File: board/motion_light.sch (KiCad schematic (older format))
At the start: 14 parts, among them CON1 AVR-ISP-6, J1 MOTION, J2 Conn_02x03_Counter_Clockwise, SW1 SW_Push, SW2 SW_Push, U1 ATTINY84-SSU, U2 APA102, U3 APA102, U4 PIR_MODULE

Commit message: Schematic revisions
* Add BoM details
* Add pull-down resistor on motion detector module
* Change GPIO header to 1x5
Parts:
- removed J2: Conn_02x03_Counter_Clockwise, Pin_Headers:Pin_Header_Straight_2x03_Pitch2.54mm, symbol Conn_02x03_Counter_Clockwise
- added J2: Conn_01x05, Pin_Headers:Pin_Header_Straight_1x05_Pitch2.54mm, symbol Conn_01x05
- added R4: 68.1K, Resistors_SMD:R_0805_HandSoldering, symbol R
- BT1: MFR (none) -> Keystone Electronics; MPN (none) -> 2464; SPN (none) -> 36-2464-ND; SPR (none) -> Digikey; SPURL (none) -> -
- CON1: MFR (none) -> Harwin Inc.; MPN (none) -> M20-9980345; SPN (none) -> 952-2120-ND; SPR (none) -> Digikey; SPURL (none) -> -
- D1: MFR (none) -> -; MPN (none) -> -; SPN (none) -> -; SPR (none) -> -; SPURL (none) -> -
- J1: MFR (none) -> Sullins Connector Solutions; MPN (none) -> PRPC040SBAN-M71RC; SPN (none) -> S1111EC-40-ND; SPR (none) -> Digikey; SPURL (none) -> -
- R1: MFR (none) -> Luna Optoelectronics; MPN (none) -> PDV-P8103; SPN (none) -> PDV-P8103-ND; SPR (none) -> Digikey; SPURL (none) -> -
- R2: MFR (none) -> Stackpole; MPN (none) -> RNCP0805FTD10K0; SPN (none) -> RNCP0805FTD10K0CT-ND; SPR (none) -> Digikey; SPURL (none) -> -
- R3: MFR (none) -> Stackpole; MPN (none) -> RNCP0805FTD1K00; SPN (none) -> RNCP0805FTD1K00CT-ND; SPR (none) -> Digikey; SPURL (none) -> -
- SW1, SW2: footprint Buttons_Switches_THT:SW_PUSH_6mm -> Buttons_Switches_THT:SW_Tactile_SPST_Angled_PTS645Vx83-2LFS; MFR (none) -> C&K; MPN (none) -> PTS645VH83-2 LFS; SPN (none) -> CKN9121-ND; SPR (none) -> Digikey; SPURL (none) -> -
- U1: value ATTINY84-SSU -> ATTINY84A-SSU; symbol ATTINY84-20SSU -> ATTINY84A-SSU; MFR (none) -> Microchip Technology; MPN (none) -> ATTINY84A-SSUR; SPN (none) -> ATTINY84A-SSURCT-ND; SPR (none) -> Digikey; SPURL (none) -> -
- U2, U3: MFR (none) -> -; MPN (none) -> APA102C; SPN (none) -> -; SPR (none) -> Ali Express; SPURL (none) -> -
- U4: MFR (none) -> Panasonic; MPN (none) -> EKMC1601111; SPN (none) -> 255-3074-ND; SPR (none) -> Digikey; SPURL (none) -> -
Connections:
- wire segments 44 -> 45

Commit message: Correct parts in BoM
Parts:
- R4: SPN RNCP0805FTD10K0CT-ND -> RNCP0805FTD68K1CT-ND
- SW1, SW2: MPN PTS645VH83-2 LFS -> PTS645VL83-2 LFS; SPN CKN9121-ND -> CKN9123-ND
- U4: MPN EKMC1601111 -> EKMC1603112; SPN 255-3074-ND -> 255-3087-ND
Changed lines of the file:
@@
 F 3 "http://www.ckswitches.com/media/1471/pts645.pdf" H 5650 950 50 0001 C CNN
 F 4 "C&K" H 0 0 50 0001 C CNN "MFR"
-F 5 "PTS645VH83-2 LFS" H 0 0 50 0001 C CNN "MPN"
-F 6 "Digikey" H 0 0 50 0001 C CNN "SPR"
-F 7 "CKN9121-ND" H 0 0 50 0001 C CNN "SPN"
+F 5 "PTS645VL83-2 LFS" H 0 0 50 0001 C CNN "MPN"
+F 6 "Digikey" H 0 0 50 0001 C CNN "SPR"
+F 7 "CKN9123-ND" H 0 0 50 0001 C CNN "SPN"
 F 8 "-" H 0 0 50 0001 C CNN "SPURL"
 	1    5650 750
@@
 F 3 "http://www3.panasonic.biz/ac/e_download/control/sensor/human/catalog/bltn_eng_papirs.pdf" H 4050 2600 60 0001 C CNN
 F 4 "Panasonic" H 0 0 50 0001 C CNN "MFR"
-F 5 "EKMC1601111" H 0 0 50 0001 C CNN "MPN"
-F 6 "Digikey" H 0 0 50 0001 C CNN "SPR"
-F 7 "255-3074-ND" H 0 0 50 0001 C CNN "SPN"
+F 5 "EKMC1603112" H 0 0 50 0001 C CNN "MPN"
+F 6 "Digikey" H 0 0 50 0001 C CNN "SPR"
+F 7 "255-3087-ND" H 0 0 50 0001 C CNN "SPN"
 F 8 "-" H 0 0 50 0001 C CNN "SPURL"
 	1    4050 2600
@@
 F 3 "http://www.ckswitches.com/media/1471/pts645.pdf" H 5650 1400 50 0001 C CNN
 F 4 "C&K" H 0 0 50 0001 C CNN "MFR"
-F 5 "PTS645VH83-2 LFS" H 0 0 50 0001 C CNN "MPN"
-F 6 "Digikey" H 0 0 50 0001 C CNN "SPR"
-F 7 "CKN9121-ND" H 0 0 50 0001 C CNN "SPN"
+F 5 "PTS645VL83-2 LFS" H 0 0 50 0001 C CNN "MPN"
+F 6 "Digikey" H 0 0 50 0001 C CNN "SPR"
+F 7 "CKN9123-ND" H 0 0 50 0001 C CNN "SPN"
 F 8 "-" H 0 0 50 0001 C CNN "SPURL"
 	1    5650 1200
@@
 F 5 "RNCP0805FTD68K1" H 0 0 50 0001 C CNN "MPN"
 F 6 "Digikey" H 0 0 50 0001 C CNN "SPR"
-F 7 "RNCP0805FTD10K0CT-ND" H 0 0 50 0001 C CNN "SPN"
+F 7 "RNCP0805FTD68K1CT-ND" H 0 0 50 0001 C CNN "SPN"
 F 8 "-" H 0 0 50 0001 C CNN "SPURL"
 	1    4500 2000

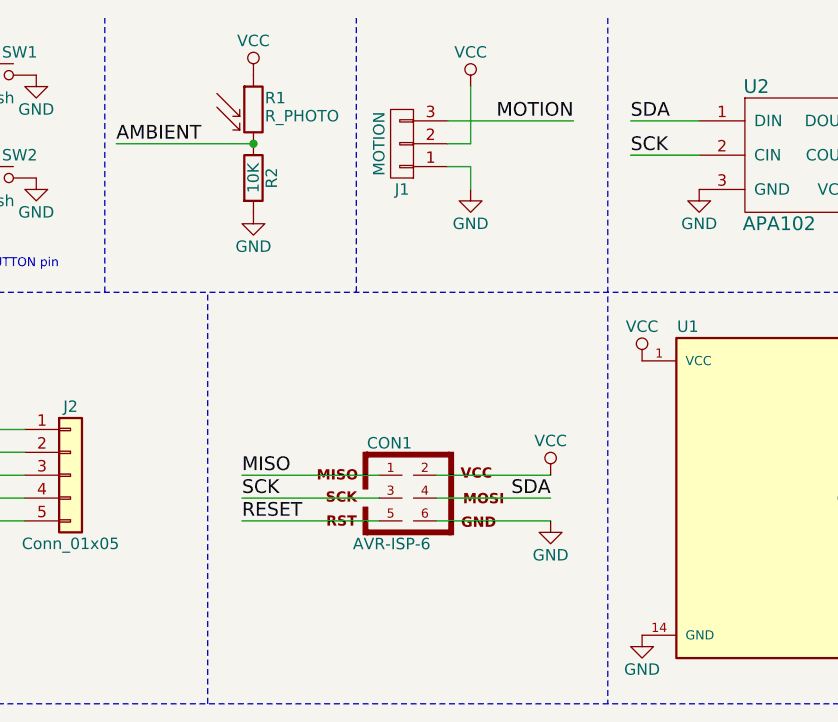
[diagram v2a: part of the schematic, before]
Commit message: Add decoupling cap
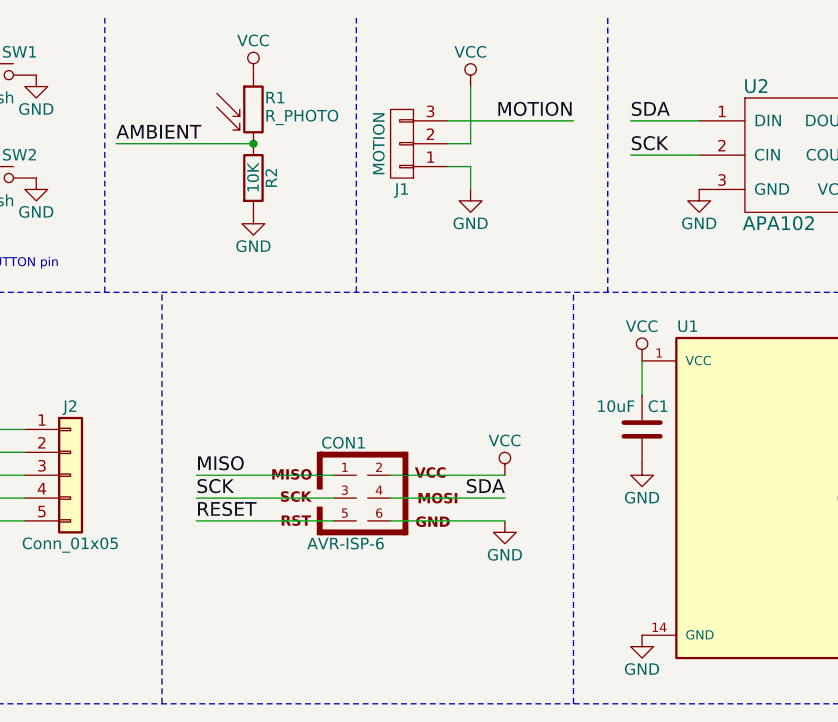
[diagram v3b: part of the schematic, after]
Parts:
- added C1: 10uF, Capacitors_SMD:C_0805_HandSoldering, symbol C
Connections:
- net GND: now also C1.2
- net VCC: now also C1.1
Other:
- moved on the sheet: CON1

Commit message: Schematic changes of unknown variety
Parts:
- added Q1: BSS83P, TO_SOT_Packages_SMD:SOT-23, symbol BSS83P
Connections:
- net VCC: now also Q1.2 (S); no longer R1.1, U2.4 (VCC), U3.4 (VCC)
- net PA3 renamed ACC_PWR
- net ACC_PWR: now also R1.1, U2.4 (VCC), U3.4 (VCC), Q1.3 (D); no longer U1.10 ((PCINT3/T0/ADC3)PA3)
- new net ~ACC_PWR_EN: Q1.1 (G), U1.10 ((PCINT3/T0/ADC3)PA3)
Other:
- moved on the sheet: C1

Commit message: Moar schematic changes
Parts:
- added J3: USB_OTG, Connectors_USB:USB_Micro-B_Molex-105017-0001, symbol USB_OTG
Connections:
- net ACC_PWR: now also J1.2 (P2), U4.1 (VDD)
- net GND: now also J3.5 (GND), J3.6 (Shield)
- net VCC: now also J3.1 (VBUS); no longer J1.2 (P2), U4.1 (VDD)
- no-connect marks 2 -> 5
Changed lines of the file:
@@
 $EndComp
 $Comp
-L GND #PWR10
+L GND #PWR01
 U 1 1 59B440F3
 P 5850 750
-F 0 "#PWR10" H 5850 500 50  0001 C CNN
+F 0 "#PWR01" H 5850 500 50  0001 C CNN
 F 1 "GND" H 5850 600 50  0000 C CNN
 F 2 "" H 5850 750 50  0001 C CNN
@@
 $EndComp
 $Comp
-L VCC #PWR17
+L VCC #PWR02
 U 1 1 59B443A5
 P 8500 2000
-F 0 "#PWR17" H 8500 1850 50  0001 C CNN
+F 0 "#PWR02" H 8500 1850 50  0001 C CNN
 F 1 "VCC" H 8500 2150 50  0000 C CNN
 F 2 "" H 8500 2000 50  0001 C CNN
@@
 $EndComp
 $Comp
-L GND #PWR18
+L GND #PWR03
 U 1 1 59B443C3
 P 8500 3200
-F 0 "#PWR18" H 8500 2950 50  0001 C CNN
+F 0 "#PWR03" H 8500 2950 50  0001 C CNN
 F 1 "GND" H 8500 3050 50  0000 C CNN
 F 2 "" H 8500 3200 50  0001 C CNN
@@
 $EndComp
 $Comp
-L VCC #PWR13
-U 1 1 59B44512
-P 7750 800
-F 0 "#PWR13" H 7750 650 50  0001 C CNN
-F 1 "VCC" H 7750 950 50  0000 C CNN
-F 2 "" H 7750 800 50  0001 C CNN
-F 3 "" H 7750 800 50  0001 C CNN
-	1    7750 800
-	1    0    0    -1
-$EndComp
-$Comp
-L GND #PWR14
+L GND #PWR04
 U 1 1 59B44548
 P 7750 1250
-F 0 "#PWR14" H 7750 1000 50  0001 C CNN
+F 0 "#PWR04" H 7750 1000 50  0001 C CNN
 F 1 "GND" H 7750 1100 50  0000 C CNN
 F 2 "" H 7750 1250 50  0001 C CNN
@@
 $EndComp
 $Comp
-L VCC #PWR15
+L VCC #PWR05
 U 1 1 59B44758
 P 7900 2500
-F 0 "#PWR15" H 7900 2350 50  0001 C CNN
+F 0 "#PWR05" H 7900 2350 50  0001 C CNN
 F 1 "VCC" H 7900 2650 50  0000 C CNN
 F 2 "" H 7900 2500 50  0001 C CNN
@@
 $EndComp
 $Comp
-L GND #PWR16
+L GND #PWR06
 U 1 1 59B44778
 P 7900 2700
-F 0 "#PWR16" H 7900 2450 50  0001 C CNN
+F 0 "#PWR06" H 7900 2450 50  0001 C CNN
 F 1 "GND" H 7900 2550 50  0000 C CNN
 F 2 "" H 7900 2700 50  0001 C CNN
@@
 $EndComp
 $Comp
-L VCC #PWR5
+L VCC #PWR07
 U 1 1 59B46B1F
 P 4550 850
-F 0 "#PWR5" H 4550 700 50  0001 C CNN
+F 0 "#PWR07" H 4550 700 50  0001 C CNN
 F 1 "VCC" H 4550 1000 50  0000 C CNN
 F 2 "" H 4550 850 50  0001 C CNN
@@
 $EndComp
 $Comp
-L GND #PWR6
+L GND #PWR08
 U 1 1 59B46B41
 P 4550 1250
-F 0 "#PWR6" H 4550 1000 50  0001 C CNN
+F 0 "#PWR08" H 4550 1000 50  0001 C CNN
 F 1 "GND" H 4550 1100 50  0000 C CNN
 F 2 "" H 4550 1250 50  0001 C CNN
@@
 $EndComp
 $Comp
-L GND #PWR12
+L GND #PWR09
 U 1 1 59B47FCA
 P 6800 1350
-F 0 "#PWR12" H 6800 1100 50  0001 C CNN
+F 0 "#PWR09" H 6800 1100 50  0001 C CNN
 F 1 "GND" H 6800 1200 50  0000 C CNN
 F 2 "" H 6800 1350 50  0001 C CNN
@@
 $EndComp
 $Comp
-L VCC #PWR8
+L VCC #PWR010
 U 1 1 59E6DA53
 P 5350 2300
-F 0 "#PWR8" H 5350 2150 50  0001 C CNN
+F 0 "#PWR010" H 5350 2150 50  0001 C CNN
 F 1 "VCC" H 5350 2450 50  0000 C CNN
 F 2 "" H 5350 2300 50  0001 C CNN
@@
 $EndComp
 $Comp
-L GND #PWR9
+L GND #PWR011
 U 1 1 59E6DA7B
 P 5350 2700
-F 0 "#PWR9" H 5350 2450 50  0001 C CNN
+F 0 "#PWR011" H 5350 2450 50  0001 C CNN
 F 1 "GND" H 5350 2550 50  0000 C CNN
 F 2 "" H 5350 2700 50  0001 C CNN
@@
 $EndComp
 $Comp
-L GND #PWR2
+L GND #PWR012
 U 1 1 59E6E9D6
 P 4100 1450
-F 0 "#PWR2" H 4100 1200 50  0001 C CNN
+F 0 "#PWR012" H 4100 1200 50  0001 C CNN
 F 1 "GND" H 4100 1300 50  0000 C CNN
 F 2 "" H 4100 1450 50  0001 C CNN
@@
 $EndComp
 $Comp
-L VCC #PWR3
-U 1 1 59E6F86C
-P 4500 2500
-F 0 "#PWR3" H 4500 2350 50  0001 C CNN
-F 1 "VCC" H 4500 2650 50  0000 C CNN
-F 2 "" H 4500 2500 50  0001 C CNN
-F 3 "" H 4500 2500 50  0001 C CNN
-	1    4500 2500
-	1    0    0    -1
-$EndComp
-$Comp
-L GND #PWR4
+L GND #PWR013
 U 1 1 59E6F89A
 P 4500 2700
-F 0 "#PWR4" H 4500 2450 50  0001 C CNN
+F 0 "#PWR013" H 4500 2450 50  0001 C CNN
 F 1 "GND" H 4500 2550 50  0000 C CNN
 F 2 "" H 4500 2700 50  0001 C CNN
@@
 $EndComp
 $Comp
-L GND #PWR11
+L GND #PWR014
 U 1 1 59E75359
 P 5850 1200
-F 0 "#PWR11" H 5850 950 50  0001 C CNN
+F 0 "#PWR014" H 5850 950 50  0001 C CNN
 F 1 "GND" H 5850 1050 50  0000 C CNN
 F 2 "" H 5850 1200 50  0001 C CNN
@@
 $EndComp
 $Comp
-L GND #PWR7
+L GND #PWR015
 U 1 1 59F51723
 P 4650 2000
-F 0 "#PWR7" H 4650 1750 50  0001 C CNN
+F 0 "#PWR015" H 4650 1750 50  0001 C CNN
 F 1 "GND" H 4650 1850 50  0000 C CNN
 F 2 "" H 4650 2000 50  0001 C CNN
@@
 	7650 950  8200 950
 Wire Wire Line
-	7650 1050 7750 1050
-Wire Wire Line
-	7750 1050 7750 800
+	7650 1050 8200 1050
 Wire Wire Line
 	7650 1150 7750 1150
@@
 	4950 1700 4950 500
 Wire Notes Line
-	3750 3500 11200 3500
+	2050 3500 11200 3500
 Wire Notes Line
 	6400 3500 6400 1700
@@
 	3950 2000 4350 2000
 Wire Wire Line
-	5800 2700 5450 2700
-Wire Wire Line
-	5450 2700 5350 2700
+	5350 2700 5800 2700
 Connection ~ 6800 1050
 Wire Wire Line
@@
 	9800 1250 9800 650
 $Comp
-L GND #PWR19
+L GND #PWR016
 U 1 1 59B441B9
 P 8750 1250
-F 0 "#PWR19" H 8750 1000 50  0001 C CNN
+F 0 "#PWR016" H 8750 1000 50  0001 C CNN
 F 1 "GND" H 8750 1100 50  0000 C CNN
 F 2 "" H 8750 1250 50  0001 C CNN
@@
 $EndComp
 $Comp
-L GND #PWR20
+L GND #PWR017
 U 1 1 59B4419D
 P 10000 1250
-F 0 "#PWR20" H 10000 1000 50  0001 C CNN
+F 0 "#PWR017" H 10000 1000 50  0001 C CNN
 F 1 "GND" H 10000 1100 50  0000 C CNN
 F 2 "" H 10000 1250 50  0001 C CNN
@@
 $EndComp
 $Comp
-L VCC #PWR1
+L VCC #PWR018
 U 1 1 5A543B0A
 P 3050 1250
-F 0 "#PWR1" H 3050 1100 50  0001 C CNN
+F 0 "#PWR018" H 3050 1100 50  0001 C CNN
 F 1 "VCC" H 3050 1400 50  0000 C CNN
 F 2 "" H 3050 1250 50  0001 C CNN
@@
 $EndComp
 Wire Wire Line
-	11050 650  9800 650
-Wire Wire Line
-	9800 650  9350 650
+	11050 650  9350 650
 Connection ~ 9800 650
 Text Label 9350 650  0    60   ~ 0
@@
 	8500 2700 8500 3200
 Wire Notes Line
-	2050 1700 2050 500
+	2050 500  2050 3500
 Text Label 5350 2400 0    60   ~ 0
 ACC_PWR
+Wire Wire Line
+	4500 2500 4850 2500
+Text Label 4850 2500 2    60   ~ 0
+ACC_PWR
+Text Label 8200 1050 2    60   ~ 0
+ACC_PWR
+$Comp
+L USB_OTG J3
+U 1 1 5A6A8C04
+P 2900 2600
+F 0 "J3" H 2700 3050 50  0000 L CNN
+F 1 "USB_OTG" H 2700 2950 50  0000 L CNN
+F 2 "Connectors_USB:USB_Micro-B_Molex-105017-0001" H 3050 2550 50  0001 C CNN
+F 3 "" H 3050 2550 50  0001 C CNN
+	1    2900 2600
+	1    0    0    -1
+$EndComp
+NoConn ~ 3200 2600
+NoConn ~ 3200 2700
+NoConn ~ 3200 2800
+$Comp
+L VCC #PWR019
+U 1 1 5A6A8D45
+P 3200 2400
+F 0 "#PWR019" H 3200 2250 50  0001 C CNN
+F 1 "VCC" H 3200 2550 50  0000 C CNN
+F 2 "" H 3200 2400 50  0001 C CNN
+F 3 "" H 3200 2400 50  0001 C CNN
+	1    3200 2400
+	1    0    0    -1
+$EndComp
+$Comp
+L GND #PWR020
+U 1 1 5A6A8DC7
+P 2900 3000
+F 0 "#PWR020" H 2900 2750 50  0001 C CNN
+F 1 "GND" H 2900 2850 50  0000 C CNN
+F 2 "" H 2900 3000 50  0001 C CNN
+F 3 "" H 2900 3000 50  0001 C CNN
+	1    2900 3000
+	1    0    0    -1
+$EndComp
+$Comp
+L GND #PWR021
+U 1 1 5A6A8DFF
+P 2800 3000
+F 0 "#PWR021" H 2800 2750 50  0001 C CNN
+F 1 "GND" H 2800 2850 50  0000 C CNN
+F 2 "" H 2800 3000 50  0001 C CNN
+F 3 "" H 2800 3000 50  0001 C CNN
+	1    2800 3000
+	1    0    0    -1
+$EndComp
 $EndSCHEMATC

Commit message: Switch to KiCAD 5; add USB plugs
* Update footprints and library symbols to KiCAD 5
* Add optional USB plugs to power directly
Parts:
- added J4: USB_MICRO, Connector_USB:USB_Micro-B_Molex-105017-0001, symbol Connector:USB_B_Micro
- BT1: symbol Battery -> Device:Battery
- C1: footprint Capacitors_SMD:C_0805_HandSoldering -> Capacitor_SMD:C_0805_2012Metric_Pad1.15x1.40mm_HandSolder; symbol C -> Device:C
- CON1: footprint Pin_Headers:Pin_Header_Straight_2x03_Pitch2.54mm -> Connector_PinHeader_2.54mm:PinHeader_2x03_P2.54mm_Vertical; symbol AVR-ISP-6 -> Connector:AVR-ISP-6
- D1: footprint LEDs:LED_0805_HandSoldering -> LED_SMD:LED_0805_2012Metric_Pad1.15x1.40mm_HandSolder; symbol LED_ALT -> Device:LED_ALT
- J1: footprint Pin_Headers:Pin_Header_Angled_1x03_Pitch2.54mm -> Connector_PinHeader_2.54mm:PinHeader_1x03_P2.54mm_Horizontal; symbol CONN_01X03 -> Connector_Generic:Conn_01x03
- J2: footprint Pin_Headers:Pin_Header_Straight_1x05_Pitch2.54mm -> Connector_PinHeader_2.54mm:PinHeader_1x05_P2.54mm_Vertical; symbol Conn_01x05 -> Connector_Generic:Conn_01x05
- J3: value USB_OTG -> USB_MICRO; footprint Connectors_USB:USB_Micro-B_Molex-105017-0001 -> Connector_USB:USB_Micro-B_Molex-105017-0001; symbol USB_OTG -> Connector:USB_B_Micro
- Q1: footprint TO_SOT_Packages_SMD:SOT-23 -> Package_TO_SOT_SMD:SOT-23; symbol BSS83P -> Transistor_FET:BSS83P
- R1: footprint Opto-Devices:Resistor_LDR_5.1x4.3_RM3.4 -> OptoDevice:R_LDR_5.1x4.3mm_P3.4mm_Vertical; symbol R_PHOTO -> Device:R_PHOTO
- R2, R3, R4: footprint Resistors_SMD:R_0805_HandSoldering -> Resistor_SMD:R_0805_2012Metric_Pad1.15x1.40mm_HandSolder; symbol R -> Device:R
- SW1, SW2: footprint Buttons_Switches_THT:SW_Tactile_SPST_Angled_PTS645Vx83-2LFS -> Button_Switch_THT:SW_Tactile_SPST_Angled_PTS645Vx83-2LFS; symbol SW_Push -> Switch:SW_Push
- U1: footprint Housings_SOIC:SOIC-14_3.9x8.7mm_Pitch1.27mm -> Package_SO:SOIC-14_3.9x8.7mm_P1.27mm; symbol ATTINY84A-SSU -> MCU_Microchip_ATtiny:ATtiny84A-SSU
- U2, U3: symbol APA102 -> crumpschemes:APA102
- U4: symbol PIR_MODULE -> steve_parts:PIR_MODULE
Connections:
- net GND: now also J4.5 (GND), J4.6 (Shield)
- net VCC: now also J4.1 (VBUS)
- no-connect marks 5 -> 8
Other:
- moved on the sheet: C1, J2, J3, U1
